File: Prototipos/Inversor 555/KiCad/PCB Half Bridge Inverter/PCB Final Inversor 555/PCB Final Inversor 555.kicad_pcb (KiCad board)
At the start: 2 copper layers, 50 x 100 mm, 31 parts, among them M5_BotL MountingHole_5.3mm_M5, M5_BotR MountingHole_5.3mm_M5, M5_TopL MountingHole_5.3mm_M5, M5_TopR MountingHole_5.3mm_M5, Q1 IRFZ44, Q2 IRFZ44, Q3 BC548, U1 TLC555xD, U2 LM7809_TO220, U3 LM358

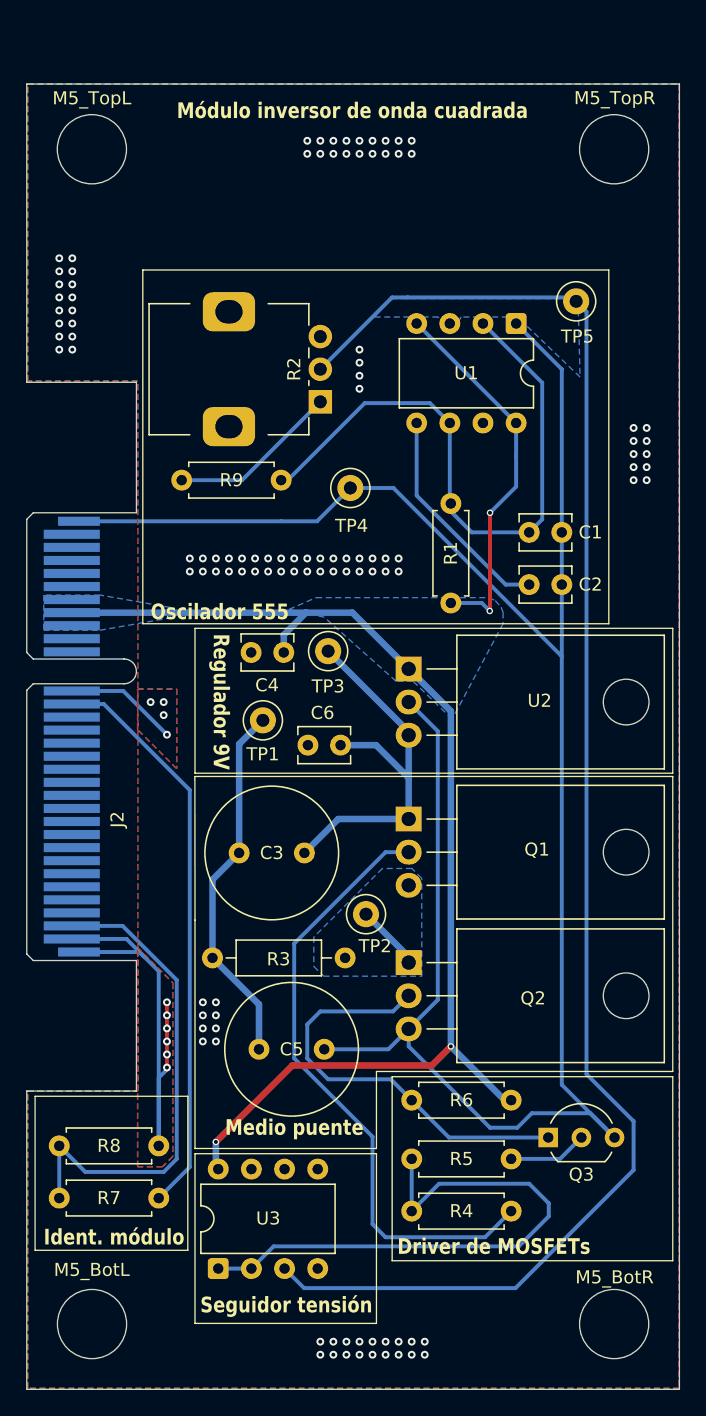
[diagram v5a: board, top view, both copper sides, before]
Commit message: Corregir módulo inversor
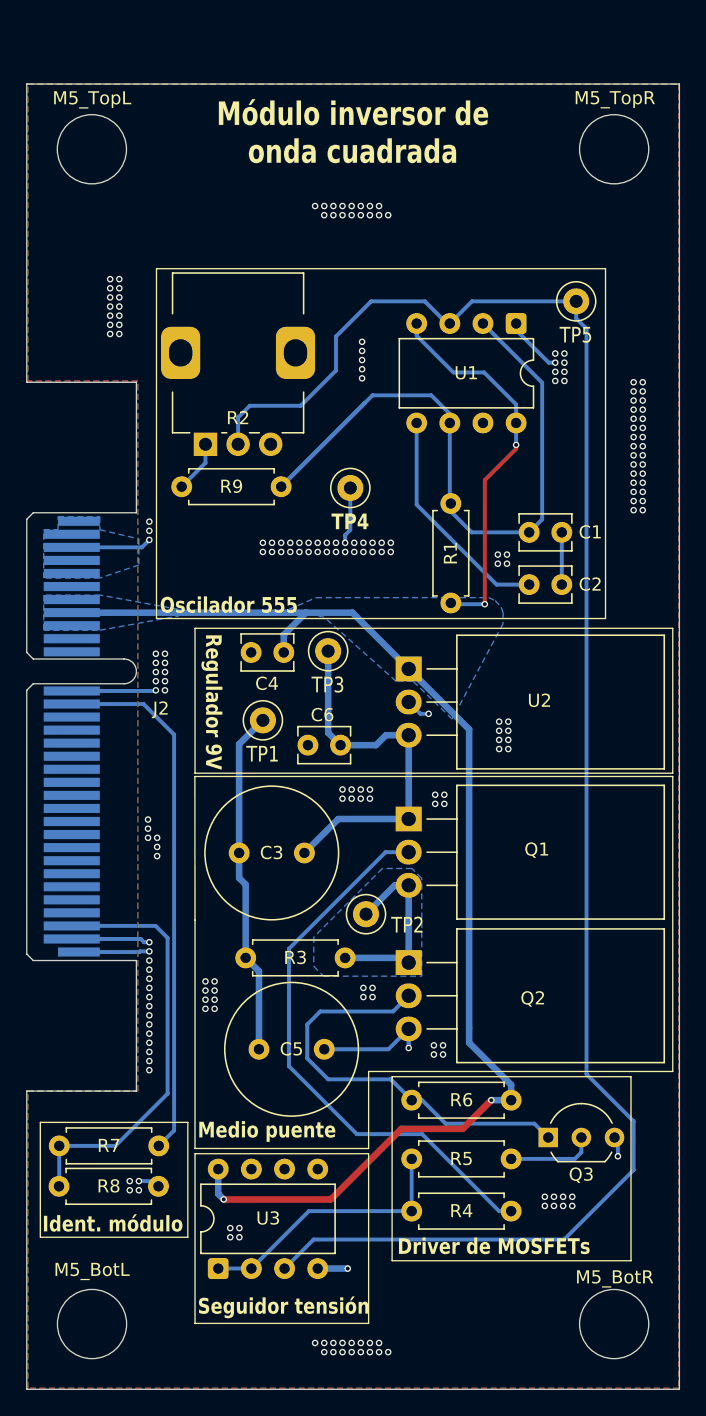
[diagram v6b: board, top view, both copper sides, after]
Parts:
- R3: value Carga -> Load; footprint Resistor_THT:R_Axial_DIN0207_L6.3mm_D2.5mm_P10.16mm_Horizontal -> Resistor_THT:R_Axial_DIN0207_L6.3mm_D2.5mm_P7.62mm_Horizontal
- TP1: value TestPoint -> Load-
- TP2: value TestPoint -> Load+
- TP3: value TestPoint -> Regulator_output
- TP4: value TestPoint -> GND
- TP5: value TestPoint -> 555_OUT
- moved R2 9.38 mm to (64.2, 75.2), turned to 90 degrees
- moved R7 4.00 mm to (60.6, 129.0)
- moved R8 3.10 mm to (53.0, 132.1)
- moved R9 0.50 mm to (70.0, 78.5)
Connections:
- C1 pad 2: PGND -> GND
- C2 pad 2: PGND -> GND
- C4 pad 2: PGND -> GND
- C5 pad 2: PGND -> GND
- C6 pad 2: PGND -> GND
- J2 pad 1: PGND -> GND
- J2 pad 2: PGND -> GND
- J2 pad 26: AGND -> GND
- J2 pad 7: AGND -> GND
- Q2 pad 3: PGND -> GND
- Q3 pad 3: PGND -> GND
- R2 pad MP: (no net) -> GND
- R8 pad 2: AGND -> GND
- TP4 pad 1: PGND -> GND
- U1 pad 1: PGND -> GND
- U2 pad 2: PGND -> GND
- U3 pad 4: PGND -> GND
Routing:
- net PGND: track 163.9 -> 0.00 mm, vias 108 -> 0
- net GND: track 0.00 -> 54.6 mm, vias 0 -> 213
- net AGND: track 46.3 -> 0.00 mm, vias 10 -> 0
- net VF_Out: track 44.0 -> 20.6 mm
- net 555: track 121.7 -> 132.8 mm
- net Net-(Q1-S): track 5.06 -> 15.6 mm
- net Net-(U1-THR): track 47.4 -> 57.3 mm
- net Net-(R2-Pad1): track 13.6 -> 4.00 mm
- net Module_ident: track 37.7 -> 32.7 mm
- net Net-(Q1-G): track 47.5 -> 42.9 mm
- net 12Vdc: track 120.8 -> 125.4 mm
- net 3,3Vdc: track 44.0 -> 40.8 mm
- net 9Vdc: track 30.7 -> 28.9 mm
- net Net-(C3-Pad2): track 28.3 -> 26.6 mm
- net Net-(Q3-B): track 6.06 -> 6.73 mm
- added copper zone on B.Cu, net GND
- added copper zone on F.Cu, net GND
- removed copper zone on B.Cu, net 555
- removed copper zone on B.Cu, net AGND
- removed copper zone on F.Cu, net AGND
- removed copper zone on B.Cu, net PGND
- removed copper zone on F.Cu, net PGND
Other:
- board text added: "Alesandria, A. S. Cignetti, M. A. Galliano, I."
- board text added: "NSH Designs"
